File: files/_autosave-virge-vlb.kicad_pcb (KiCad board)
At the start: 4 copper layers, 240.5 x 70.4 mm, 61 parts, among them J1 VLB_slot, J2 VGA, J3 VESA feature, U1 86C325, U10 74LS245, U2 27C010, Y1 14.318MHz

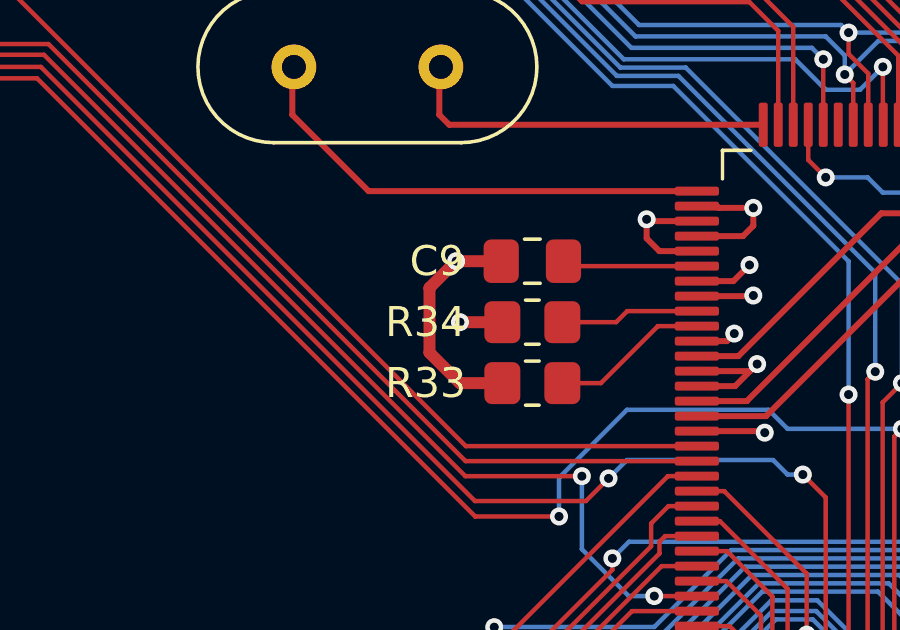
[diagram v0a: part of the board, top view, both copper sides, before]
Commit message: added VREF R for fine tuning
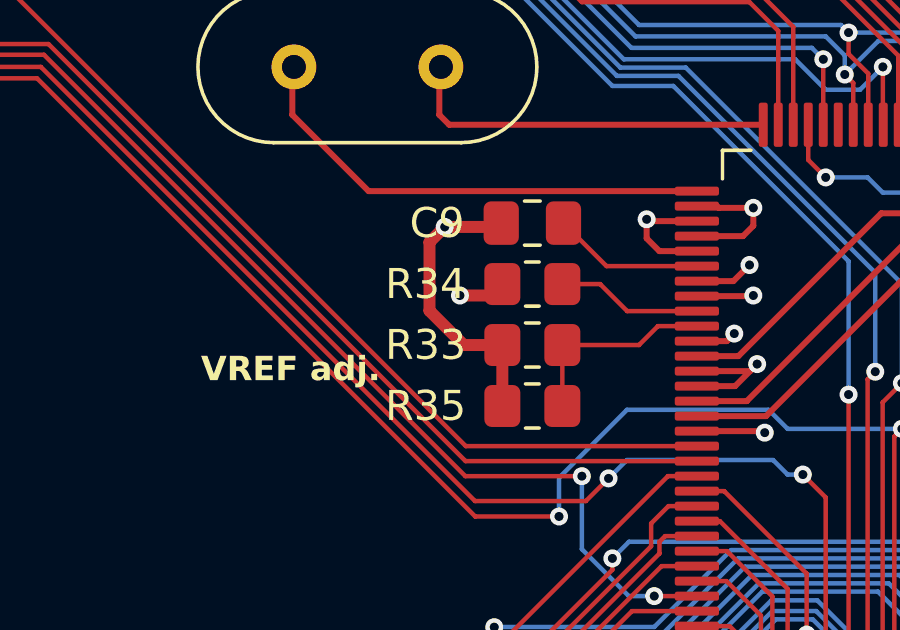
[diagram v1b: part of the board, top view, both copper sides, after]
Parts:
- added R35: ADJ, Resistor_SMD:R_0805_2012Metric_Pad1.20x1.40mm_HandSolder, F.Cu at (88.9, 111.1)
- moved C9 1.27 mm to (88.9, 105.0)
- moved R33 1.27 mm to (88.9, 109.1)
- moved R34 1.27 mm to (88.9, 107.1)
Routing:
- net GND: track 232.3 -> 234.4 mm
- net Net-(U1H-RSET): track 5.27 -> 6.78 mm
- net Net-(U1H-VREF): track 4.51 -> 5.04 mm
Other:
- board text added: "VREF adj."
